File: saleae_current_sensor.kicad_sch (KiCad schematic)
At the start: 44 parts, among them J1 USB4505-03-0-A_REVA, J2 TSM-104-02-T-DH, M1 MountingHole_Pad, M2 MountingHole_Pad, M3 MountingHole_Pad, U1 TES_1-0523, U2 L78L12, U3 L7912, U4 ACS723xLCTR-05AB, U5 ACS723xLCTR-40AB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

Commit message: Misc updates kibuzzard lock in mounting holes/connectors change dielectric thickness for total 1.6mm stackup CI updates
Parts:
- C1, C4, C5, C8: PN (none) -> CL31B475KAHNNNE
- C10, C11, C12, C15, C16, C17, C18, C6, C7, C9: PN (none) -> CL10B104KB8NNNC
- C13, C14, H1, H2, JP1, JP2, M1, M2, M3: PN (none) -> DNP
- C2, C3: PN (none) -> CL31B105KBHNNNE
- D1: PN (none) -> SZYY1206YG
- J1: PN (none) -> USB4505-03-0-A
- J2: PN (none) -> TSM-104-02-T-DH-A
- R1: PN (none) -> RC0603FR-072KL
- R2, R3: PN (none) -> RC0603FR-075K1L
- R4, R5: PN (none) -> RC0603FR-074K7L
- R6, R7: value 4.95K -> 5K; PN (none) -> AR03BTCX5001
- U1: PN (none) -> TES_1-0523
- U2: PN (none) -> L78L12ACUTR
- U3: value L7912 -> L79L12; PN (none) -> L79L12ACUTR
- U4: PN (none) -> ACS723LLCTR-05AB-T
- U5: PN (none) -> ACS723LLCTR-40AU-T
- U6, U7: PN (none) -> LT6015IS5#TRPBF
- U8, U9: PN (none) -> AD8422
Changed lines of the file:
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@@
+      (effects (font (size 1.27 1.27)) hide)
+    )
+    (property "PN" "CL10B104KB8NNNC" (at 97.79 53.34 0)
       (effects (font (size 1.27 1.27)) hide)
     )
@@
       (effects (font (size 1.27 1.27)) hide)
     )
+    (property "PN" "CL10B104KB8NNNC" (at 229.87 123.19 0)
+      (effects (font (size 1.27 1.27)) hide)
+    )
     (pin "1")
     (pin "2")
@@
     )
     (property "Datasheet" "~" (at 179.07 146.05 0)
+      (effects (font (size 1.27 1.27)) hide)
+    )
+    (property "PN" "DNP" (at 179.07 146.05 0)
       (effects (font (size 1.27 1.27)) hide)
     )
@@
       (effects (font (size 1.27 1.27)) hide)
     )
+    (property "PN" "LT6015IS5#TRPBF" (at 242.57 209.55 0)
+      (effects (font (size 1.27 1.27)) hide)
+    )
     (pin "2")
     (pin "5")
@@
       (effects (font (size 1.27 1.27)) hide)
     )
+    (property "PN" "CL10B104KB8NNNC" (at 97.79 33.02 0)
+      (effects (font (size 1.27 1.27)) hide)
+    )
     (pin "1")
     (pin "2")
@@
     )
     (property "Datasheet" "https://www.analog.com/media/en/technical-documentation/data-sheets/AD8422.pdf" (at 289.56 143.51 0)
+      (effects (font (size 1.27 1.27)) hide)
+    )
+    (property "PN" "AD8422" (at 280.67 133.35 0)
       (effects (font (size 1.27 1.27)) hide)
     )
@@
       (effects (font (size 1.27 1.27)) hide)
     )
+    (property "PN" "RC0603FR-072KL" (at 54.61 146.05 0)
+      (effects (font (size 1.27 1.27)) hide)
+    )
     (pin "1")
     (pin "2")
@@
       (effects (font (size 1.27 1.27)) (justify right))
     )
-    (property "Value" "4.95K" (at 261.62 134.62 0)
+    (property "Value" "5K" (at 265.43 134.62 0)
       (effects (font (size 1.27 1.27)) (justify right))
     )
@@
       (effects (font (size 1.27 1.27)) hide)
     )
+    (property "PN" "AR03BTCX5001" (at 269.24 133.35 0)
+      (effects (font (size 1.27 1.27)) hide)
+    )
     (pin "1")
     (pin "2")
@@
       (effects (font (size 1.27 1.27)) hide)
     )
+    (property "PN" "CL10B104KB8NNNC" (at 294.64 50.8 0)
+      (effects (font (size 1.27 1.27)) hide)
+    )
     (pin "1")
     (pin "2")
@@
     )
     (property "Datasheet" "~" (at 26.67 43.18 0)
+      (effects (font (size 1.27 1.27)) hide)
+    )
+    (property "PN" "CL31B475KAHNNNE" (at 26.67 43.18 0)
       (effects (font (size 1.27 1.27)) hide)
     )
@@
       (effects (font (size 1.27 1.27)) hide)
     )
+    (property "PN" "DNP" (at 252.73 146.05 0)
+      (effects (font (size 1.27 1.27)) hide)
+    )
     (pin "1")
     (pin "2")
@@
     (property "MANUFACTURER" "GCT" (at 36.83 101.6 0)
       (effects (font (size 1.27 1.27)) (justify left bottom) hide)
+    )
+    (property "PN" "USB4505-03-0-A" (at 36.83 101.6 0)
+      (effects (font (size 1.27 1.27)) hide)
     )
     (pin "A1_B12")
@@
       (effects (font (size 1.27 1.27)) hide)
     )
+    (property "PN" "LT6015IS5#TRPBF" (at 242.57 181.61 0)
+      (effects (font (size 1.27 1.27)) hide)
+    )
     (pin "2")
     (pin "5")
@@
       (effects (font (size 1.27 1.27)))
     )
-    (property "Value" "L7912" (at 87.63 62.23 0)
+    (property "Value" "L79L12" (at 87.63 62.23 0)
       (effects (font (size 1.27 1.27)))
     )
@@
       (effects (font (size 1.27 1.27)) hide)
     )
+    (property "PN" "L79L12ACUTR" (at 85.09 58.42 0)
+      (effects (font (size 1.27 1.27)) hide)
+    )
     (pin "1")
     (pin "2")
@@
       (effects (font (size 1.27 1.27)) (justify right))
     )
-    (property "Value" "4.95K" (at 261.62 77.47 0)
+    (property "Value" "5K" (at 265.43 77.47 0)
       (effects (font (size 1.27 1.27)) (justify right))
     )
@@
     )
     (property "Datasheet" "~" (at 269.24 76.2 0)
+      (effects (font (size 1.27 1.27)) hide)
+    )
+    (property "PN" "AR03BTCX5001" (at 269.24 76.2 0)
       (effects (font (size 1.27 1.27)) hide)
     )
@@
     (property "PARTREV" "R" (at 369.57 78.74 0)
       (effects (font (size 1.27 1.27)) (justify bottom) hide)
+    )
+    (property "PN" "TSM-104-02-T-DH-A" (at 369.57 78.74 0)
+      (effects (font (size 1.27 1.27)) hide)
     )
     (pin "01")
@@
       (effects (font (size 1.27 1.27)) hide)
     )
+    (property "PN" "DNP" (at 60.96 187.96 0)
+      (effects (font (size 1.27 1.27)) hide)
+    )
     (pin "1")
     (instances
@@
       (effects (font (size 1.27 1.27)) hide)
     )
+    (property "PN" "CL31B105KBHNNNE" (at 68.58 45.72 0)
+      (effects (font (size 1.27 1.27)) hide)
+    )
     (pin "1")
     (pin "2")
@@
     )
     (property "Datasheet" "~" (at 215.9 185.42 0)
+      (effects (font (size 1.27 1.27)) hide)
+    )
+    (property "PN" "CL10B104KB8NNNC" (at 215.9 185.42 0)
       (effects (font (size 1.27 1.27)) hide)
     )
@@
     (property "MAXIMUM_PACKAGE_HEIGHT" "7.5mm" (at 53.34 43.18 0)
       (effects (font (size 1.27 1.27)) (justify bottom) hide)
+    )
+    (property "PN" "TES_1-0523" (at 53.34 43.18 0)
+      (effects (font (size 1.27 1.27)) hide)
     )
     (pin "1")
@@
       (effects (font (size 1.27 1.27)) hide)
     )
+    (property "PN" "SZYY1206YG" (at 54.61 138.43 0)
+      (effects (font (size 1.27 1.27)) hide)
+    )
     (pin "1")
     (pin "2")
@@
     )
     (property "Datasheet" "~" (at 294.64 115.57 0)
+      (effects (font (size 1.27 1.27)) hide)
+    )
+    (property "PN" "CL10B104KB8NNNC" (at 294.64 115.57 0)
       (effects (font (size 1.27 1.27)) hide)
     )
@@
       (effects (font (size 1.27 1.27)) hide)
     )
+    (property "PN" "DNP" (at 71.12 187.96 0)
+      (effects (font (size 1.27 1.27)) hide)
+    )
     (pin "1")
     (instances
@@
       (effects (font (size 1.27 1.27)) hide)
     )
+    (property "PN" "CL31B475KAHNNNE" (at 81.28 91.44 0)
+      (effects (font (size 1.27 1.27)) hide)
+    )
     (pin "1")
     (pin "2")
@@
       (effects (font (size 1.27 1.27)) hide)
     )
+    (property "PN" "CL10B104KB8NNNC" (at 229.87 66.04 0)
+      (effects (font (size 1.27 1.27)) hide)
+    )
     (pin "1")
     (pin "2")
@@
       (effects (font (size 1.27 1.27)) hide)
     )
+    (property "PN" "RC0603FR-075K1L" (at 68.58 102.87 0)
+      (effects (font (size 1.27 1.27)) hide)
+    )
     (pin "1")
     (pin "2")
@@
       (effects (font (size 1.27 1.27)) hide)
     )
+    (property "PN" "DNP" (at 179.07 81.28 0)
+      (effects (font (size 1.27 1.27)) hide)
+    )
     (pin "1")
     (instances
@@
       (effects (font (size 1.27 1.27)) hide)
     )
+    (property "PN" "CL31B475KAHNNNE" (at 101.6 91.44 0)
+      (effects (font (size 1.27 1.27)) hide)
+    )
     (pin "1")
     (pin "2")
@@
       (effects (font (size 1.27 1.27)) hide)
     )
+    (property "PN" "DNP" (at 330.2 78.74 0)
+      (effects (font (size 1.27 1.27)) hide)
+    )
     (pin "1")
     (pin "2")
@@
       (effects (font (size 1.27 1.27)) hide)
     )
+    (property "PN" "CL31B105KBHNNNE" (at 68.58 40.64 0)
+      (effects (font (size 1.27 1.27)) hide)
+    )
     (pin "1")
     (pin "2")
@@
       (effects (font (size 1.27 1.27)) hide)
     )
+    (property "PN" "CL10B104KB8NNNC" (at 215.9 214.63 0)
+      (effects (font (size 1.27 1.27)) hide)
+    )
     (pin "1")
     (pin "2")
@@
     )
     (property "Datasheet" "~" (at 294.64 58.42 0)
+      (effects (font (size 1.27 1.27)) hide)
+    )
+    (property "PN" "CL10B104KB8NNNC" (at 294.64 58.42 0)
       (effects (font (size 1.27 1.27)) hide)
     )
@@
       (effects (font (size 1.27 1.27)) hide)
     )
+    (property "PN" "DNP" (at 50.8 187.96 0)
+      (effects (font (size 1.27 1.27)) hide)
+    )
     (pin "1")
     (instances
@@
     )
     (property "Datasheet" "http://www.allegromicro.com/~/media/Files/Datasheets/ACS723-Datasheet.ashx?la=en" (at 222.25 86.36 0)
+      (effects (font (size 1.27 1.27)) hide)
+    )
+    (property "PN" "ACS723LLCTR-05AB-T" (at 222.25 86.36 0)
       (effects (font (size 1.27 1.27)) hide)
     )
@@
       (effects (font (size 1.27 1.27)) hide)
     )
+    (property "PN" "DNP" (at 330.2 73.66 0)
+      (effects (font (size 1.27 1.27)) hide)
+    )
     (pin "1")
     (pin "2")
@@
     )
     (property "Datasheet" "https://www.analog.com/media/en/technical-documentation/data-sheets/AD8422.pdf" (at 289.56 86.36 0)
+      (effects (font (size 1.27 1.27)) hide)
+    )
+    (property "PN" "AD8422" (at 280.67 76.2 0)
       (effects (font (size 1.27 1.27)) hide)
     )
@@
       (effects (font (size 1.27 1.27)) hide)
     )
+    (property "PN" "RC0603FR-074K7L" (at 256.54 88.9 0)
+      (effects (font (size 1.27 1.27)) hide)
+    )
     (pin "1")
     (pin "2")
@@
       (effects (font (size 1.27 1.27)) hide)
     )
+    (property "PN" "L78L12ACUTR" (at 85.09 27.94 0)
+      (effects (font (size 1.27 1.27)) hide)
+    )
     (pin "1")
     (pin "2")
@@
     )
     (property "Datasheet" "~" (at 294.64 107.95 0)
+      (effects (font (size 1.27 1.27)) hide)
+    )
+    (property "PN" "CL10B104KB8NNNC" (at 294.64 107.95 0)
       (effects (font (size 1.27 1.27)) hide)
     )
@@
       (effects (font (size 1.27 1.27)) hide)
     )
+    (property "PN" "RC0603FR-075K1L" (at 66.04 102.87 0)
+      (effects (font (size 1.27 1.27)) hide)
+    )
     (pin "1")
     (pin "2")
@@
       (effects (font (size 1.27 1.27)) hide)
     )
+    (property "PN" "DNP" (at 252.73 88.9 0)
+      (effects (font (size 1.27 1.27)) hide)
+    )
     (pin "1")
     (pin "2")
@@
     )
     (property "Datasheet" "http://www.allegromicro.com/~/media/Files/Datasheets/ACS723-Datasheet.ashx?la=en" (at 222.25 143.51 0)
+      (effects (font (size 1.27 1.27)) hide)
+    )
+    (property "PN" "ACS723LLCTR-40AU-T" (at 222.25 143.51 0)
       (effects (font (size 1.27 1.27)) hide)
     )
@@
       (effects (font (size 1.27 1.27)) hide)
     )
+    (property "PN" "RC0603FR-074K7L" (at 256.54 146.05 0)
+      (effects (font (size 1.27 1.27)) hide)
+    )
     (pin "1")
     (pin "2")
@@
       (effects (font (size 1.27 1.27)) hide)
     )
+    (property "PN" "CL31B475KAHNNNE" (at 91.44 91.44 0)
+      (effects (font (size 1.27 1.27)) hide)
+    )

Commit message: Final changes for JLCPCB order
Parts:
- C13, C14: now not fitted
- H1, H2, JP1, JP2, M1, M2, M3: now left out of the parts list
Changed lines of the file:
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@@
   )
   (symbol (lib_id "Mechanical:MountingHole_Pad") (at 179.07 146.05 90) (unit 1)
-    (in_bom yes) (on_board yes) (dnp no)
+    (in_bom no) (on_board yes) (dnp no)
     (property "Reference" "H2" (at 173.99 146.05 90)
       (effects (font (size 1.27 1.27)))
@@
   )
   (symbol (lib_id "Device:C_Small") (at 252.73 146.05 0) (mirror x) (unit 1)
-    (in_bom yes) (on_board yes) (dnp no) (fields_autoplaced)
+    (in_bom yes) (on_board yes) (dnp yes) (fields_autoplaced)
     (property "Reference" "C14" (at 250.19 144.7735 0)
       (effects (font (size 1.27 1.27)) (justify right))
@@
   )
   (symbol (lib_id "Mechanical:MountingHole_Pad") (at 60.96 187.96 0) (unit 1)
-    (in_bom yes) (on_board yes) (dnp no) (fields_autoplaced)
+    (in_bom no) (on_board yes) (dnp no) (fields_autoplaced)
     (property "Reference" "M2" (at 63.5 185.4199 0)
       (effects (font (size 1.27 1.27)) (justify left))
@@
   )
   (symbol (lib_id "Mechanical:MountingHole_Pad") (at 71.12 187.96 0) (unit 1)
-    (in_bom yes) (on_board yes) (dnp no) (fields_autoplaced)
+    (in_bom no) (on_board yes) (dnp no) (fields_autoplaced)
     (property "Reference" "M3" (at 73.66 185.4199 0)
       (effects (font (size 1.27 1.27)) (justify left))
@@
   )
   (symbol (lib_id "Mechanical:MountingHole_Pad") (at 179.07 81.28 90) (unit 1)
-    (in_bom yes) (on_board yes) (dnp no)
+    (in_bom no) (on_board yes) (dnp no)
     (property "Reference" "H1" (at 173.99 81.28 90)
       (effects (font (size 1.27 1.27)))
@@
   )
   (symbol (lib_id "Jumper:SolderJumper_2_Bridged") (at 330.2 78.74 0) (unit 1)
-    (in_bom yes) (on_board yes) (dnp no)
+    (in_bom no) (on_board yes) (dnp no)
     (property "Reference" "JP2" (at 330.2 81.28 0)
       (effects (font (size 1.27 1.27)))
@@
   )
   (symbol (lib_id "Mechanical:MountingHole_Pad") (at 50.8 187.96 0) (unit 1)
-    (in_bom yes) (on_board yes) (dnp no) (fields_autoplaced)
+    (in_bom no) (on_board yes) (dnp no) (fields_autoplaced)
     (property "Reference" "M1" (at 53.34 185.4199 0)
       (effects (font (size 1.27 1.27)) (justify left))
@@
   )
   (symbol (lib_id "Jumper:SolderJumper_2_Bridged") (at 330.2 73.66 0) (unit 1)
-    (in_bom yes) (on_board yes) (dnp no)
+    (in_bom no) (on_board yes) (dnp no)
     (property "Reference" "JP1" (at 330.2 71.12 0)
       (effects (font (size 1.27 1.27)))
@@
   )
   (symbol (lib_id "Device:C_Small") (at 252.73 88.9 0) (mirror x) (unit 1)
-    (in_bom yes) (on_board yes) (dnp no) (fields_autoplaced)
+    (in_bom yes) (on_board yes) (dnp yes) (fields_autoplaced)
     (property "Reference" "C13" (at 250.19 87.6235 0)
       (effects (font (size 1.27 1.27)) (justify right))

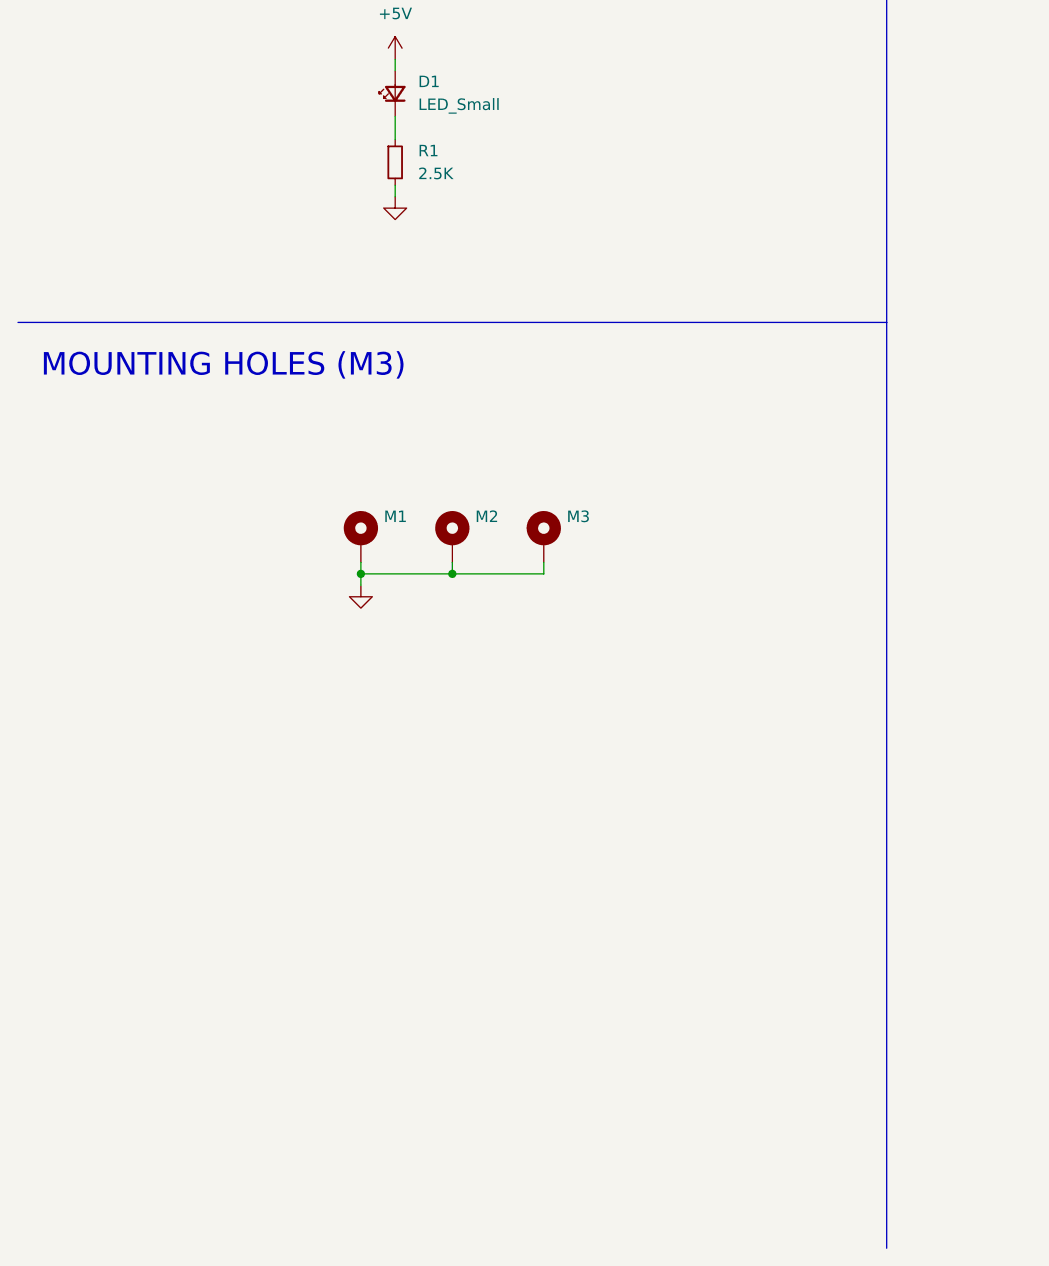
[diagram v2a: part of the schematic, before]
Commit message: Add 2V5 voltage reference :( and reduce LED resistor
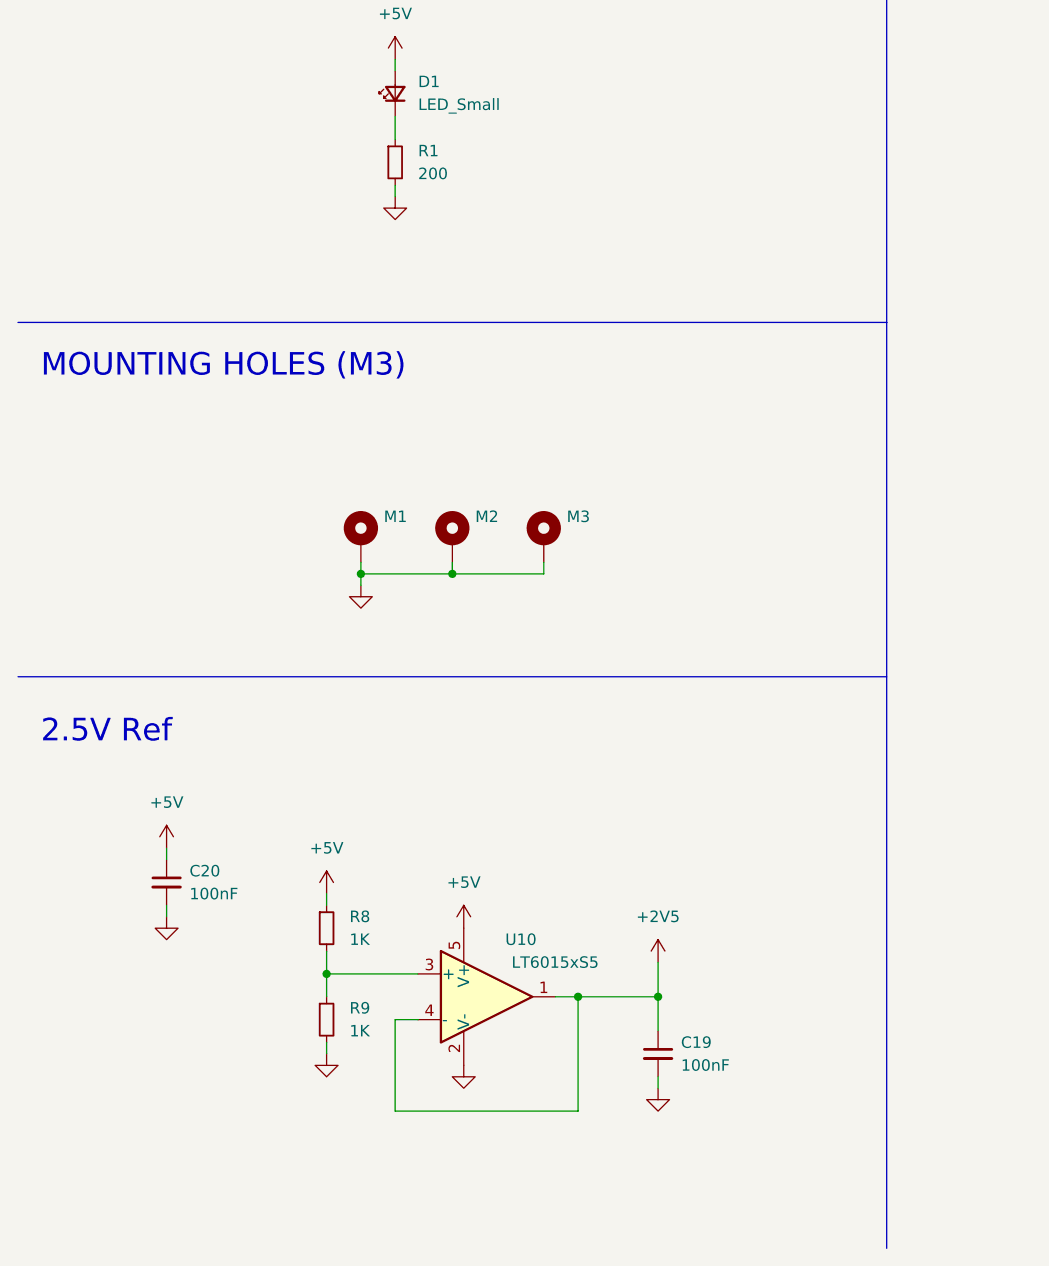
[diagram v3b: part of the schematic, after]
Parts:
- added C19, C20: 100nF, Capacitor_SMD:C_0603_1608Metric, symbol Device:C_Small
- added R8, R9: 1K, Resistor_SMD:R_0603_1608Metric, symbol Device:R_Small
- added U10: LT6015xS5, Package_TO_SOT_SMD:SOT-23-5, symbol Amplifier_Operational:LT6015xS5
- R1: value 2.5K -> 200; PN RC0603FR-072KL -> RC0603FR-07200RL
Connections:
- net +2V5: now also C19.1, U10.1, U10.4 (-)
- net +5V: now also C20.1, R8.1, U10.5 (V+)
- net GND: now also C19.2, C20.2, R9.2, U10.2 (V-)
- new net: R8.2, R9.1, U10.3 (+)
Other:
- note added: "2.5V Ref"
